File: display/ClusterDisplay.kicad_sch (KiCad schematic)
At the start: 72 parts, among them J1 Verdin iMX95, J10 RTC coin cell, J2 Power in, J3 CAN to ECU, J4 DM-TFTR50-413 panel, J8 JTAG debug, J9 Buttons, Q1 NFET diode, Q2 NFET pass, Q3 MFT6N2A5S23A (AEC-Q101, 60V/2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, U1 LM74930-Q1, U2 LM61460-Q1, U3 TLV767-Q1, U4 TCAN1044V-Q1, U6 TPS60403-Q1, U7 AL8853AQ

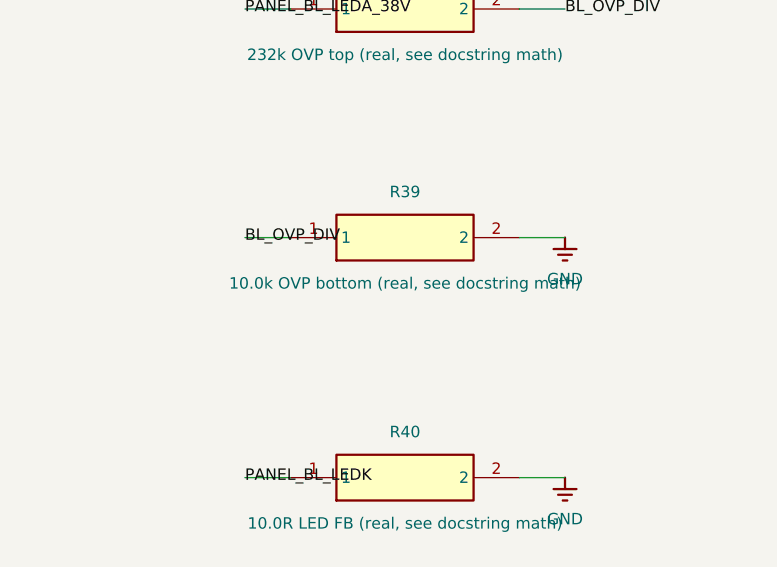
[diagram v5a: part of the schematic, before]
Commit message: display: route board and generate real BOM
Added +12V_PROT trunk-widening constants (TRUNK_WIDTH_LADDER/
TRUNK_NETS) to build_pcb.py - this board's own real fused/protected
rail, feeding both the main +5V buck and the backlight boost converter,
so it's sized toward F1's real 5A rating rather than reusing gauges/'s
smaller 2A-fuse ladder.

Routed ClusterDisplay.kicad_pcb with FreeRouting (0 unrouted on the
first attempt) plus post-route GND/+5V zone pours (this board has no
+3V3 net - +5V is the real widely-distributed second rail here) and
+12V_PROT trunk widening, adapted from gauges/route_board.py. Same real
TRACK_CLEARANCE fix applied (0.15 -> 0.2, see gauges/route_board.py's
own comment for the full real DRC evidence).

Fixed a real value-spelling bug caught by build_bom.py's own check:
R39 was written as "10.0k" while the identical 10k pullups (R21, R44-
R48) were written "10k" - same real part, split into two BOM lines by
spelling alone. Normalized to "10k" (the OVP divider's ~25% real
margin doesn't call for a tighter tolerance than the default), then
regenerated schematic -> PCB -> re-routed (footprint/net-only pipeline,
reproduced the identical 105.0x106.0mm layout as expected).

Added build_bom.py, same real generated-BOM discipline as gauges/'s
own - this board has more genuine "needs real part selection" lines
(Q1/Q2 front-end FETs, D1 TVS, F1's exact fuse suffix, J1's exact
Verdin SKU, J2/J3/J8/J9's provisional headers) since the AAOS pivot
that created it only landed 2 days ago; each is flagged honestly
rather than given a fabricated-precise part number. 72/72 real parts
covered (after fixing a real multi-unit-symbol double-count in
load_parts() - J1's Verdin X1 connector is split into 7 real schematic
units sharing one Reference, which a naive one-entry-per-symbol-
instance count would silently double-count 7x).

Co-Authored-By: Claude Sonnet 5 <noreply@anthropic.com>
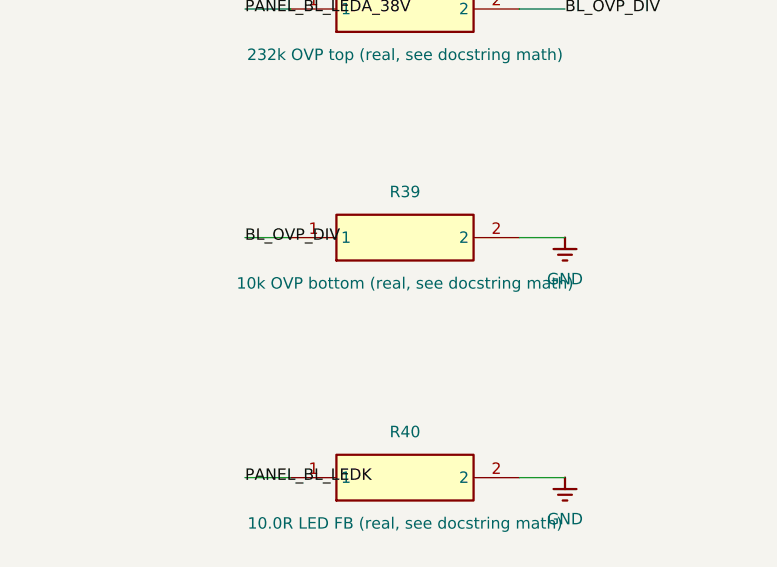
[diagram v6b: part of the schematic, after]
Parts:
- R39: value 10.0k OVP bottom (real, see docstring math) -> 10k OVP bottom (real, see docstring math)

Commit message: display: resolve 5 of 9 TBD BOM lines with real, cited parts
Real part selection, each one researched and verified against its own
real datasheet rather than guessed:

- Q1/Q2 (front-end back-to-back FET pair): Nexperia PMV55ENEA (60V,
  VGS +-20V, 3.1A, SOT-23, AEC-Q101). Selected directly against
  LM74930-Q1's own datasheet (SNOSDF6) "MOSFET Q2 Selection" section,
  which states two real requirements: 60V VDS (matching this board's
  real single-TVS front end) and >=15V VGS rating (HGATE/DGATE can
  drive up to 14V) - PMV55ENEA satisfies both with real margin.
  Honestly flagged: its 3.1A continuous rating sits below F1's own 5A
  hold current; real steady-state current draw hasn't been
  independently verified against its SOA curve.
- D1 (input TVS): SMCJ33A - the same real part gauges/'s own front end
  already uses for the identical role.
- F1 (input fuse): Bourns MF-RG500, replacing MF-RG300. Real, not
  cosmetic: MF-RG300 (this board's footprint until now) is genuinely a
  3.0A-hold part per Bourns' own real datasheet, while the circuit's
  own target was 5A - MF-RG500 is the correct family member, with its
  own real (larger) physical package, confirmed against KiCad's
  bundled Fuse_Bourns_MF-RG500 footprint.
- J1 (Verdin SoM): real, confirmed-orderable Toradex product name
  "Verdin iMX95 Hexa 8GB WB IT" (independently listed on Mouser US and
  UK) - Hexa/8GB for real Android Automotive headroom, IT to match
  every other automotive-grade part on this board. Toradex's own
  internal order code still needs confirming at purchase time.

Regenerated schematic -> PCB -> re-routed (0 unrouted, confirmed by
real DRC via route_board.py's own new verification step) -> BOM.
Board size essentially unchanged (105.0x106.0 -> 104.8x106.0mm).

Remaining open: J2/J3/J8/J9, 4 provisional pin-header connectors -
genuinely can't be picked without knowing the real harness/enclosure
design, left open deliberately rather than guessed at.

Co-Authored-By: Claude Sonnet 5 <nore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
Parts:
- D1: value TVS 33V -> SMCJ33A
- F1: value 5A -> MF-RG500 (Bourns, 5.0A hold/8.5A trip, AEC-Q200); footprint Fuse:Fuse_Bourns_MF-RG300 -> Fuse:Fuse_Bourns_MF-RG500
- J1: value Verdin iMX95 -> Verdin iMX95 Hexa 8GB WB IT
- Q1: value NFET diode -> PMV55ENEA (AEC-Q101, 60V/20V VGS) diode
- Q2: value NFET pass -> PMV55ENEA (AEC-Q101, 60V/20V VGS) pass

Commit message: display: switch to the 800-nit TSD TST040HDBC-42 round panel
The 350-nit DM-TFTR50-413 washes out in sun, is rated only -20..60C, and its
127mm circle would be cropped by the 105.5mm dash opening. New panel: 4in,
800 nits, -30..80C, 101.5mm active circle. Adds TPS65131-Q1 +/-6.5V rails,
TPS61165-Q1 15V/180mA backlight with PWM dimming, Hirose FH26 FPC connector,
real harness connectors J2/J3/J8/J9, and open solder jumpers for the panel's
datasheet-conflicting +/-6.5V pin polarity. Re-routed (0 unconnected), BOM
regenerated. Also adds the website dashboard graphic under media/.

Co-Authored-By: Claude Sonnet 5.5 <noreply@anthropic.com>
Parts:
- removed C40: 1u Cfly (AEC-Q200), Capacitor_SMD:C_0603_1608Metric, symbol ClusterDisplay:C
- removed C41: 1u CI (AEC-Q200), Capacitor_SMD:C_0603_1608Metric, symbol ClusterDisplay:C
- removed L2: 680u boost inductor (real, see docstring math), Inductor_SMD:L_1210_3225Metric, symbol ClusterDisplay:L
- removed Q3: MFT6N2A5S23A (AEC-Q101, 60V/2.5A), Package_TO_SOT_SMD:SOT-23, symbol ClusterDisplay:NFET
- removed U6: TPS60403-Q1, Package_TO_SOT_SMD:SOT-23-5, symbol ClusterDisplay:TPS60403-Q1
- removed U7: AL8853AQ, Package_SO:SOIC-8_3.9x4.9mm_P1.27mm, symbol ClusterDisplay:AL8853AQ
- added C40: 4.7u boost in (AEC-Q200), Capacitor_SMD:C_0805_2012Metric, symbol ClusterDisplay:C_0805
- added C41: 4.7u inverter in (AEC-Q200), Capacitor_SMD:C_0805_2012Metric, symbol ClusterDisplay:C_0805
- added C46: 22u VPOS out 16V (AEC-Q200), Capacitor_SMD:C_1206_3216Metric, symbol ClusterDisplay:C_1206
- added C47: 22u VNEG out 16V (AEC-Q200), Capacitor_SMD:C_1206_3216Metric, symbol ClusterDisplay:C_1206
- added C48: 12p VPOS feed-forward (AEC-Q200), Capacitor_SMD:C_0603_1608Metric, symbol ClusterDisplay:C
- added C49: 15p VNEG feed-forward (AEC-Q200), Capacitor_SMD:C_0603_1608Metric, symbol ClusterDisplay:C
- added C50: 10u BL input (AEC-Q200), Capacitor_SMD:C_0805_2012Metric, symbol ClusterDisplay:C_0805
- added C51: 220n BL COMP (AEC-Q200), Capacitor_SMD:C_0603_1608Metric, symbol ClusterDisplay:C
- added C52: 10u BL output 25V (AEC-Q200), Capacitor_SMD:C_1206_3216Metric, symbol ClusterDisplay:C_1206
- added D3, D4: PMEG6010ELRX (AEC-Q101, 60V/1A), Diode_SMD:Nexperia_CFP3_SOD-123W, symbol ClusterDisplay:SCHOTTKY_SOD123W
- added JP1: SJ3 OPEN: bridge 1-2 if datasheet TABLE is right 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, Jumper:SolderJumper-3_P1.3mm_Open_RoundedPad1.0x1.5mm, symbol ClusterDisplay:SOLDERJUMPER3
- added JP2: SJ3 OPEN: bridge 2-3 if datasheet TABLE is right 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, Jumper:SolderJumper-3_P1.3mm_Open_RoundedPad1.0x1.5mm, symbol ClusterDisplay:SOLDERJUMPER3
- added L2: 4.7u boost (Coilcraft XAL4030-472ME), Inductor_SMD:L_Coilcraft_XAL4030-XXX, symbol ClusterDisplay:L_4U7
- added L3: 4.7u inverter (Coilcraft XAL4030-472ME), Inductor_SMD:L_Coilcraft_XAL4030-XXX, symbol ClusterDisplay:L_4U7
- added L4: 10u BL boost (Coilcraft XAL4040-103ME), Inductor_SMD:L_Coilcraft_XAL4040-XXX, symbol ClusterDisplay:L_10U
- added R41: 100k VNEG bottom R4 to VREF (see docstring), Resistor_SMD:R_0603_1608Metric, symbol ClusterDisplay:R
- added R42: 1.10R LED current sense (0.2V/1.10=182mA), Resistor_SMD:R_0603_1608Metric, symbol ClusterDisplay:R
- added R43: 100k bias-enable pulldown, Resistor_SMD:R_0603_1608Metric, symbol ClusterDisplay:R
- added R50: 100k panel-reset pulldown, Resistor_SMD:R_0603_1608Metric, symbol ClusterDisplay:R
- added U6: TPS65131-Q1, Package_DFN_QFN:HVQFN-24-1EP_4x4mm_P0.5mm_EP2.5x2.5mm, symbol ClusterDisplay:TPS65131-Q1
- added U7: TPS61165-Q1, Package_TO_SOT_SMD:SOT-23-6, symbol ClusterDisplay:TPS61165-Q1
- C42: value 1u CO (AEC-Q200) -> 100n VIN filter (AEC-Q200)
- C43: value 1u VIN (AEC-Q200) -> 220n VREF (AEC-Q200)
- C44: value 10n COMP (typical, not loop-verified) -> 10n CP comp (AEC-Q200)
- C45: value 1u VOUT, 63V-rated (AEC-Q200) -> 4n7 CN comp (AEC-Q200)
- J2: value Power in -> Phoenix MKDS 1,5/3-5,08 power in (DTM06-3S pigtail); footprint Connector_PinHeader_2.54mm:PinHeader_1x03_P2.54mm_Vertical -> TerminalBlock_Phoenix:TerminalBlock_Phoenix_MKDS-1,5-3-5.08_1x03_P5.08mm_Horizontal
- J3: value CAN to ECU -> Molex KK-254 22-27-2031 CAN (DTM06-3S pigtail); footprint Connector_PinHeader_2.54mm:PinHeader_1x03_P2.54mm_Vertical -> Connector_Molex:Molex_KK-254_AE-6410-03A_1x03_P2.54mm_Vertical
- J4: value DM-TFTR50-413 panel -> TST040HDBC-42 panel; footprint Connector_Hirose_DF40:Hirose_DF40C-50DP-0.4V_2x25-1MP_P0.4mm -> Connector_FFC-FPC:Hirose_FH26-39S-0.3SHW_2Rows-39Pins-1MP_P0.60mm_Horizontal
- J8: value JTAG debug -> Samtec TSW-108-07-G-S JTAG (bench only)
- J9: value Buttons -> Samtec TSW-104-07-G-S buttons (bench only)
- R37: value 2.00R OCP/CS sense (real, see docstring math) -> 100R VIN filter
- R38: value 232k OVP top (real, see docstring math) -> 562k VPOS top R1 (see docstring)
- R39: value 10k OVP bottom (real, see docstring math) -> 130k VPOS bottom R2 (see docstring)
- R40: value 10.0R LED FB (real, see docstring math) -> 536k VNEG top R3 (see docstring)
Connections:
- net BL_CS_NODE is gone; now on net +5V: R37.1
- net +12V_PROT: no longer C43.1
- net +1V8: now also J4.13 (IOVCC), J4.14 (IOVCC); no longer J4.22 (IOVCC), J4.24 (IOVCC)
- net +5V: now also C40.1, C41.1, C50.1, L2.1, L4.1, U6.5 (INN1), U6.6 (INN2), U7.1 (VIN); no longer J4.36 (VSP), J4.38 (VSP)
- net BL_COMP: now also C51.1, U7.5 (COMP); no longer C44.1
- net BL_SW: now also D4.2, L4.2, U7.3 (SW); no longer D2.1
- net DSI_CLK_N: now also J4.30 (CLK_N); no longer J4.17 (CLK_N)
- net DSI_CLK_P: now also J4.28 (CLK_P); no longer J4.15 (CLK_P)
- net DSI_D0_N: now also J4.38 (LAN0_N); no longer J4.23 (LAN0_N)
- net DSI_D0_P: now also J4.36 (LAN0_P); no longer J4.21 (LAN0_P)
- net DSI_D1_N: now also J4.34 (LAN1_N); no longer J4.11 (LAN1_N)
- net DSI_D1_P: now also J4.32 (LAN1_P); no longer J4.9 (LAN1_P)
- net DSI_D2_N: now also J4.26 (LAN2_N); no longer J4.5 (LAN2_N)
- net DSI_D2_P: now also J4.24 (LAN2_P); no longer J4.3 (LAN2_P)
- net DSI_PANEL_EN: now also J4.16 (RESET), R50.1; no longer J4.48 (RESET)
- net GND: now also J4.12 (GND), J4.15 (GND), J4.17 (GND), J4.23 (GND), J4.27 (GND), J4.35 (GND), J4.39 (GND), J4.6 (GND), J4.9 (GND), C40.2, C41.2, C46.2, C47.2, C50.2, C51.2, C52.2, L3.2, R42.2, R43.2, R50.2, U6.11 (PSN), U6.19 (AGND), U6.2 (PGND1), U6.25 (EP), U6.3 (PGND2), U6.9 (PSP), U7.4 (GND); no longer J4.13 (GND), J4.14 (GND), J4.2 (GND), J4.20 (GND), J4.25 (GND), J4.26 (GND), J4.37 (GND), J4.42 (GND), J4.47 (GND), J4.49 (GND), J4.50 (GND), J4.7 (GND), J4.8 (GND), R37.2, R40.2
- net PANEL_BL_LEDK: now also J4.5 (LEDK), R42.1, U7.6 (FB); no longer J4.6 (LEDK), R40.1
- net PANEL_BL_PWM: now reaches J1.19 (PWM_3_DSI)
- net PANEL_BL_PWM: now also U7.2 (CTRL)
- net PANEL_BIAS_EN: now reaches J1.21 (GPIO_10_DSI)
- net PANEL_BIAS_EN: now also R43.1, U6.10 (ENN), U6.8 (ENP)
- net BL_OVP_DIV renamed PANEL_FBP
- net PANEL_FBP: now also C48.2, U6.22 (FBP)
- net DSI_D3_N: no longer names the net of J1.23 (DSI_1_D3_N)
- net DSI_D3_N: no longer J4.29 (LAN3_N)
- net DSI_D3_P: no longer names the net of J1.25 (DSI_1_D3_P)
- net DSI_D3_P: no longer J4.27 (LAN3_P)
- removed net PANEL_BL_LEDA_38V: C45.1, D2.2, J4.10 (LEDA), J4.12 (LEDA), R38.1
- removed net PANEL_VSN_NEG5V: C42.1, J4.30 (VSN), J4.32 (VSN)
- new net PANEL_BIAS_VIN: C42.1, R37.2, U6.4 (VIN)
- new net PANEL_BL_LEDA: C52.1, D4.1, J4.2 (LEDA), J4.3 (LEDA)
- new net PANEL_BOOST_SW: D2.2, L2.2, U6.1 (INP1), U6.24 (INP2)
- new net PANEL_CN: C45.1, U6.18 (CN)
- new net PANEL_CP: C44.1, U6.21 (CP)
- new net PANEL_FBN: C49.2, R40.2, R41.1, U6.16 (FBN)
- new net PANEL_INV_SW: D3.1, L3.1, U6.13 (OUTN1), U6.14 (OUTN2)
- new net PANEL_PIN_A: J4.7 (VPIN_A), J4.8 (VPIN_A), JP1.2 (COM)
- new net PANEL_PIN_B: J4.10 (VPIN_B), J4.11 (VPIN_B), JP2.2 (COM)
- new net PANEL_VREF: C43.1, R41.2, U6.17 (VREF)
- new net PANEL_VSN: C47.1, C49.1, D3.2, JP1.3 (B), JP2.3 (B), R40.1, U6.15 (VNEG)
- new net PANEL_VSP: C46.1, C48.1, D2.1, JP1.1 (A), JP2.1 (A), R38.1, U6.23 (VPOS)
- no-connect marks 198 -> 200
